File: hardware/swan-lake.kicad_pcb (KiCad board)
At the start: 2 copper layers, 22.9 x 22.9 mm, 2 parts, among them IC1 ATTINY85-S, P1 CONN_01X08

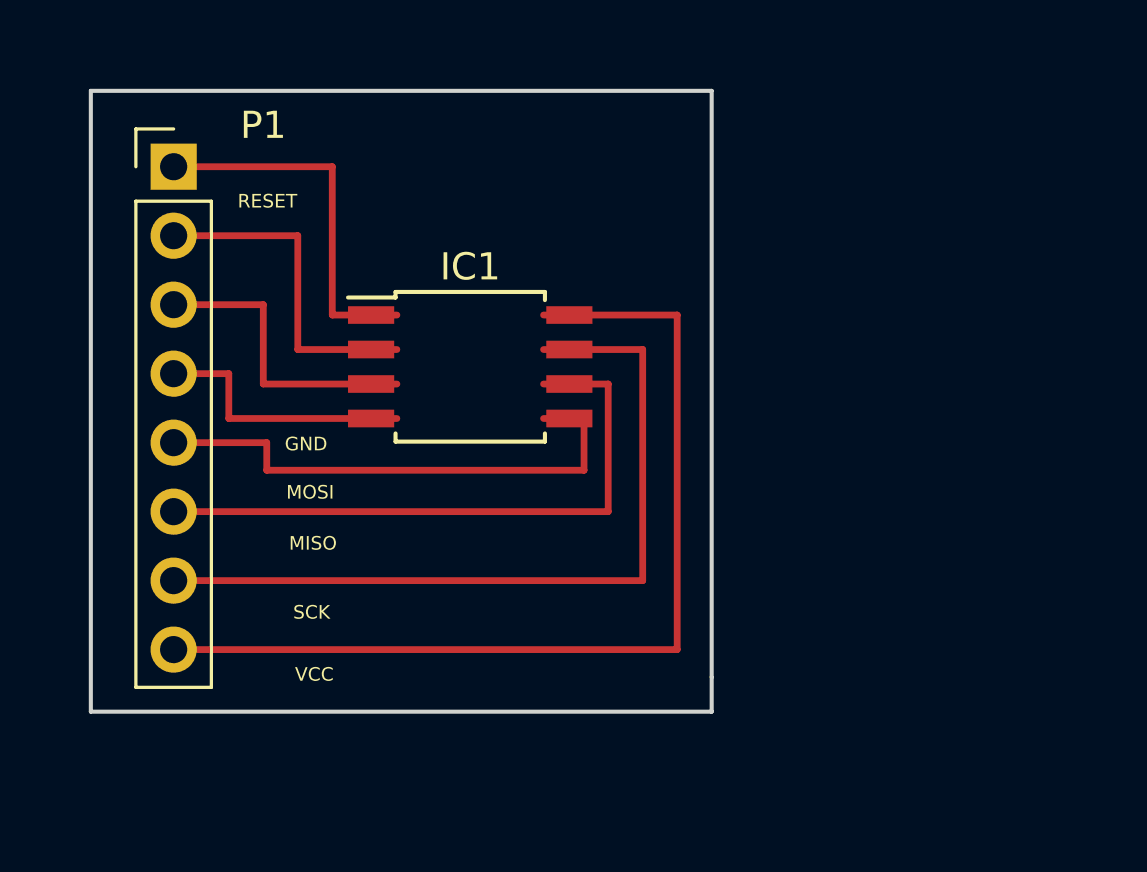
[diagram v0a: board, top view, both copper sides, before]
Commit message: Add PCB layout for etching
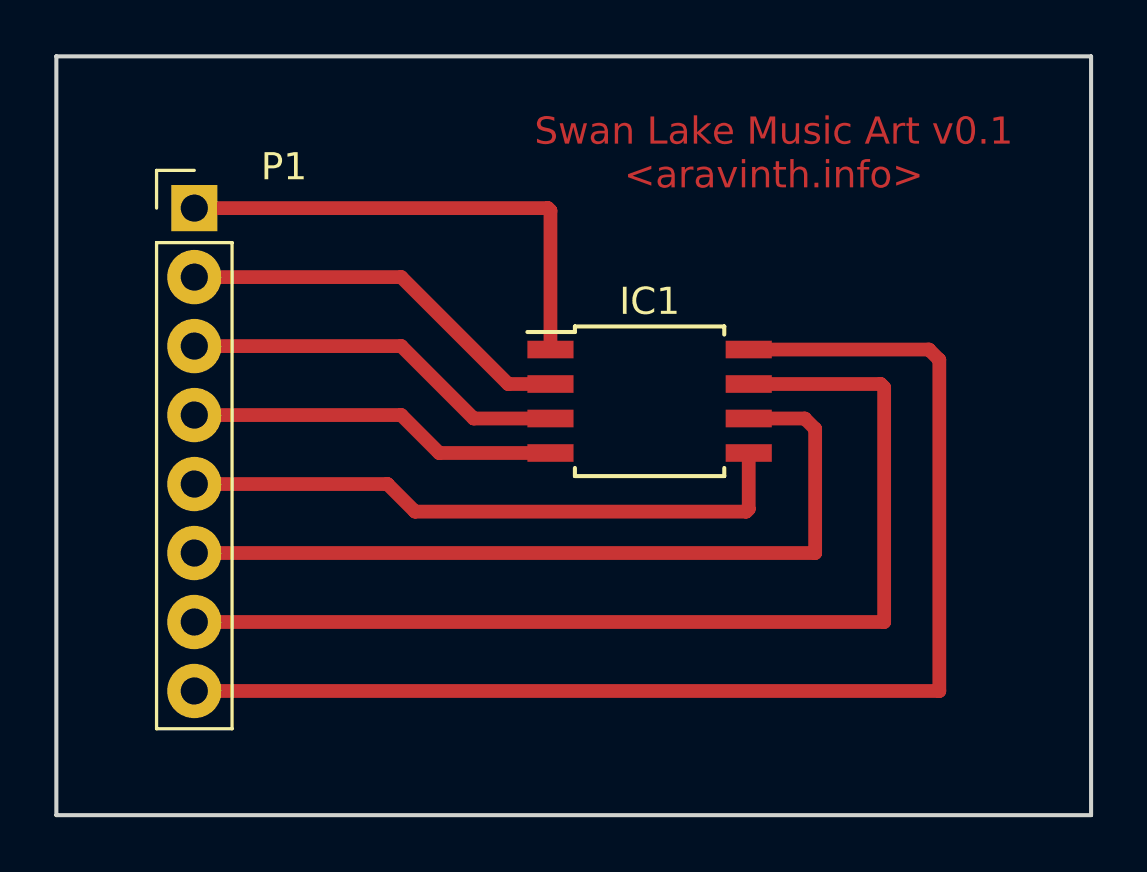
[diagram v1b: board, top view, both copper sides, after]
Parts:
- moved IC1 6.73 mm to (174.2, 119.4)
- moved P1 1.70 mm to (157.5, 112.3)
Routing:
- net Net-(IC1-Pad8): track 35.8 -> 46.8 mm
- net Net-(IC1-Pad7): track 29.4 -> 39.1 mm
- net Net-(IC1-Pad6): track 23.1 -> 30.0 mm
- net Net-(IC1-Pad1): track 13.7 -> 18.3 mm
- net Net-(IC1-Pad4): track 9.87 -> 13.7 mm
- net Net-(IC1-Pad5): track 19.5 -> 22.9 mm
- net Net-(IC1-Pad3): track 11.1 -> 14.2 mm
- net Net-(IC1-Pad2): track 12.4 -> 14.7 mm
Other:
- board size 22.9 x 22.9 mm -> 38.1 x 27.9 mm
- net class Default: trace_width 0.25 -> 0.508
- board text added: "Swan Lake Music Art v0.1 <aravinth.info>"
- board text removed: "GND"
- board text removed: "MISO"
- board text removed: "MOSI"
- board text removed: "RESET"
- board text removed: "SCK"
- board text removed: "VCC"
